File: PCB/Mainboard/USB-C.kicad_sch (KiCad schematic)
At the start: 21 parts, among them J1 TYPE-C-31-M-12, Q1 AON7262E, Q2 AON7262E, U3 TPD4E05U06DQA

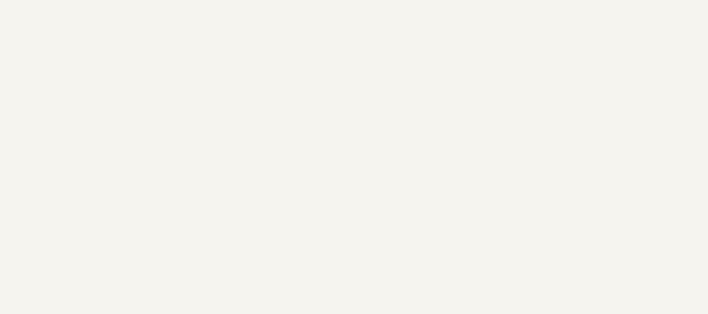
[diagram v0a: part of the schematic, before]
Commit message: Added setup, read and get Command
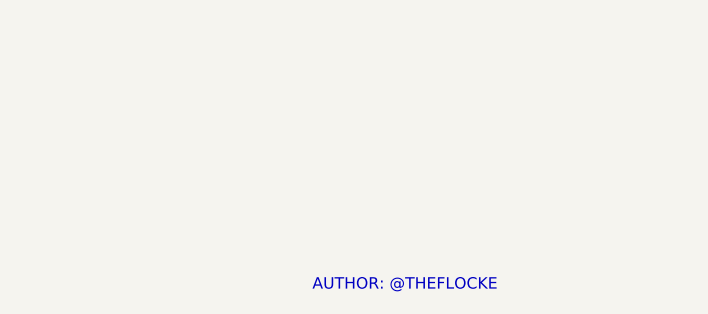
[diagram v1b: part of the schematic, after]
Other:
- note added: "AUTHOR: @THEFLOCKE"
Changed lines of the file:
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@@
+		)
+	)
+	(text "AUTHOR: @THEFLOCKE"
+		(exclude_from_sim no)
+		(at 249.936 196.596 0)
+		(effects
+			(font
+				(face "KiCad Font")
+				(size 1.27 1.27)
+				(color 194 0 194 1)
+			)
 		)
 	)

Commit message: Fixed Grammar
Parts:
- removed C5, C7: 100nF, Capacitor_SMD:C_0805_2012Metric_Pad1.18x1.45mm_HandSolder, symbol Device:C
- removed C6, C9: 10uF, Capacitor_SMD:C_0805_2012Metric_Pad1.18x1.45mm_HandSolder, symbol Device:C
- removed C8: 1uF, Capacitor_SMD:C_0805_2012Metric_Pad1.18x1.45mm_HandSolder, symbol Device:C
- removed D1, D2: LED, Diode_SMD:D_0805_2012Metric_Pad1.15x1.40mm_HandSolder, symbol Device:LED
- removed D3: 100V, Diode_SMD:D_SMA, symbol Device:D_Schottky
- removed J1: TYPE-C-31-M-12, Footprints:HRO_TYPE-C-31-M-12, symbol TYPE-C-31-M-12:TYPE-C-31-M-12
- removed Q1, Q2: AON7262E, AON7262E, symbol AON7262E:AON7262E
- removed R10, R12: 10k, Resistor_SMD:R_0805_2012Metric_Pad1.20x1.40mm_HandSolder, symbol Device:R
- removed R11: 10m, Resistor_SMD:R_0805_2012Metric_Pad1.20x1.40mm_HandSolder, symbol Device:R
- removed R6, R7, R8, R9: 5k1, Resistor_SMD:R_0805_2012Metric_Pad1.20x1.40mm_HandSolder, symbol Device:R
- removed TH1: NTC-10k, Resistor_SMD:R_0805_2012Metric_Pad1.20x1.40mm_HandSolder, symbol Device:Thermistor_NTC
- removed U2: ~, custom:AP33772, symbol Custom:AP33772
- removed U3: TPD4E05U06DQA, Package_SON:USON-10_2.5x1.0mm_P0.5mm, symbol Power_Protection:TPD4E05U06DQA
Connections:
- no-connect marks 8 -> 0
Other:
- note removed: "I2C ADRESS: 0x51"

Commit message: upload images and deleted pcb new
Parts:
- added C5, C7: 100nF, Capacitor_SMD:C_0805_2012Metric_Pad1.18x1.45mm_HandSolder, symbol Device:C
- added C6, C9: 10uF, Capacitor_SMD:C_0805_2012Metric_Pad1.18x1.45mm_HandSolder, symbol Device:C
- added C8: 1uF, Capacitor_SMD:C_0805_2012Metric_Pad1.18x1.45mm_HandSolder, symbol Device:C
- added D1, D2: LED, Diode_SMD:D_0805_2012Metric_Pad1.15x1.40mm_HandSolder, symbol Device:LED
- added D3: 100V, Diode_SMD:D_SMA, symbol Device:D_Schottky
- added J1: TYPE-C-31-M-12, Footprints:HRO_TYPE-C-31-M-12, symbol TYPE-C-31-M-12:TYPE-C-31-M-12
- added Q1, Q2: AON7262E, AON7262E, symbol AON7262E:AON7262E
- added R10, R12: 10k, Resistor_SMD:R_0805_2012Metric_Pad1.20x1.40mm_HandSolder, symbol Device:R
- added R11: 10m, Resistor_SMD:R_0805_2012Metric_Pad1.20x1.40mm_HandSolder, symbol Device:R
- added R6, R7, R8, R9: 5k1, Resistor_SMD:R_0805_2012Metric_Pad1.20x1.40mm_HandSolder, symbol Device:R
- added TH1: NTC-10k, Resistor_SMD:R_0805_2012Metric_Pad1.20x1.40mm_HandSolder, symbol Device:Thermistor_NTC
- added U2: ~, custom:AP33772, symbol Custom:AP33772
- added U3: TPD4E05U06DQA, Package_SON:USON-10_2.5x1.0mm_P0.5mm, symbol Power_Protection:TPD4E05U06DQA
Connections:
- new net: D1.2 (A), R10.1
- new net: D2.2 (A), R12.1
- new net: Q1.10 (D_6), Q1.11 (D_7), Q1.5 (D_1), Q1.6 (D_2), Q1.7 (D_3), Q1.8 (D_4), Q1.9 (D_5), Q2.10 (D_6), Q2.11 (D_7), Q2.5 (D_1), Q2.6 (D_2), Q2.7 (D_3), Q2.8 (D_4), Q2.9 (D_5)
- new net: C5.1, U2.15 (IFB)
- new net: U2.10 (NC), U2.18 (NC), U2.19 (NC), U2.2 (NC), U2.21 (NC)
- new net: C7.1, U2.12 (V3VD)
- new net: TH1.1, U2.13 (OTP)
- new net: C8.1, U2.20 (V5V)
- new net CC1: J1.A5 (CC1), R6.2, U2.17 (CC1), U3.4 (D2+)
- new net CC2: J1.B5 (CC2), R9.2, U2.16 (CC2), U3.5 (D2-)
- new net GND: C5.2, C6.2, C7.2, C8.2, C9.2, D1.1 (K), D2.1 (K), D3.2 (A), J1.A1_B12 (GND), J1.B1_A12 (GND), J1.S1 (SHIELD), J1.S2 (SHIELD), J1.S3 (SHIELD), J1.S4 (SHIELD), R6.1, R9.1, TH1.2, U2.3 (GND), U3.3 (GND), U3.8 (GND)
- new net PD_INT: U2.9 (GPIO3)
- new net PD_SCL: R7.1, U2.5 (SCL)
- new net PD_SDA: R8.1, U2.4 (SDA)
- new net PWR_EN: Q1.4 (G), Q2.4 (G), U2.23 (PWR_EN)
- new net USB_D+: J1.A6 (DP1), J1.B6 (DP2), U3.1 (D1+)
- new net USB_D-: J1.A7 (DN1), J1.B7 (DN2), U3.2 (D1-)
- new net VBUS_C: C9.1, D3.1 (K), Q2.1 (S_1), Q2.2 (S_2), Q2.3 (S_3), R12.2, U2.22 (VBUS)
- new net VBUS_D: C6.1, J1.A4_B9 (VBUS), J1.B4_A9 (VBUS), R10.2, R11.1, U2.1 (ISENP)
- new net VCC: Q1.1 (S_1), Q1.2 (S_2), Q1.3 (S_3), R11.2, U2.24 (VCC)
- new net VCC_3V3: R7.2, R8.2
- no-connect marks 0 -> 8
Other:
- note added: "I2C ADRESS: 0x51"
